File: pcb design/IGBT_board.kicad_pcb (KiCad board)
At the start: 6 copper layers, 150 x 100 mm, 170 parts, among them J1 4-794627-0, Q1 IGBT, Q10 IGBT, Q11 IGBT, Q12 IGBT, Q13 NPN, Q14 PNP, Q15 CSD19533Q5A, Q16 CSD19533Q5A, Q17 NPN, Q18 PNP, Q2 IGBT, Q3 IGBT, Q4 IGBT, Q5 IGBT, Q6 IGBT, Q7 IGBT, Q8 IGBT, Q9 IGBT, T1 TRANS-3-1CT, U1 ISO5852S, U2 LM5030, U3 ISO5852S

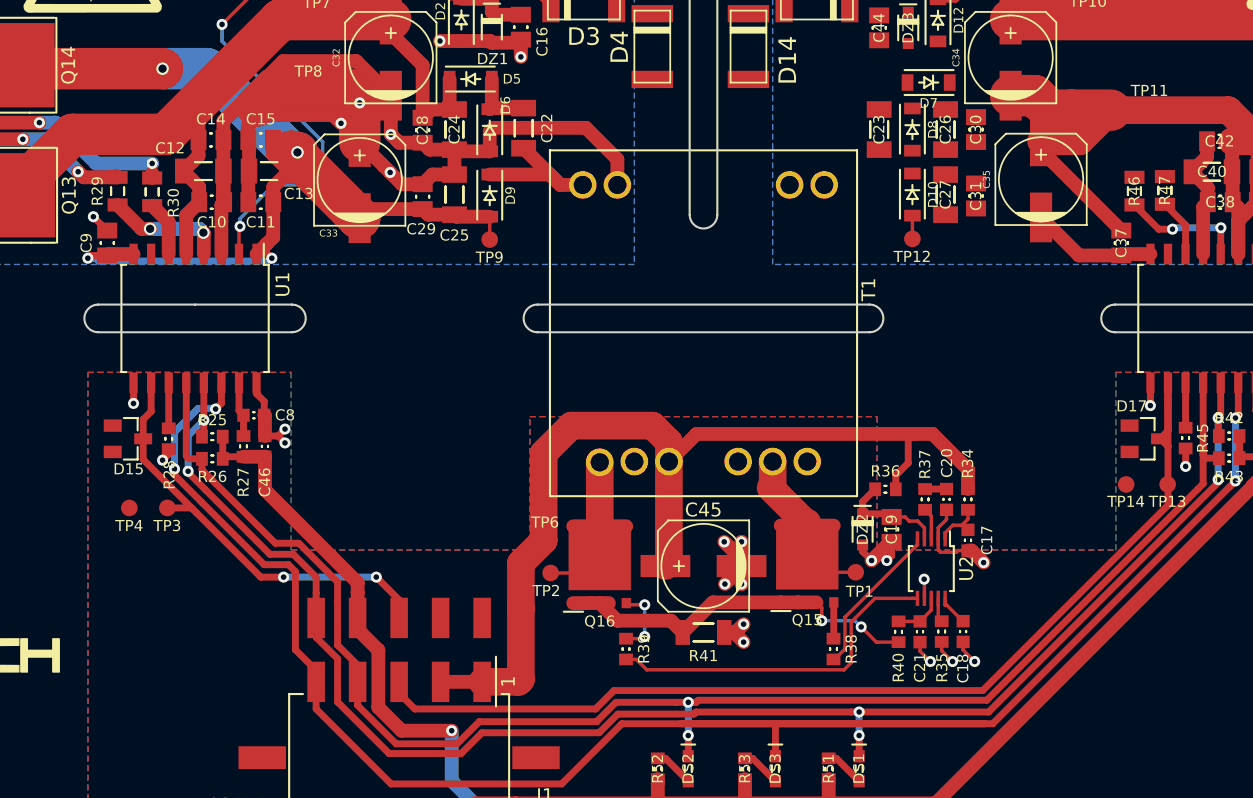
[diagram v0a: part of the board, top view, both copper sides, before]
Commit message: Sync layout with schematic
Signed-off-by: Marcos Chaparro <mchaparro@paltatech.com>
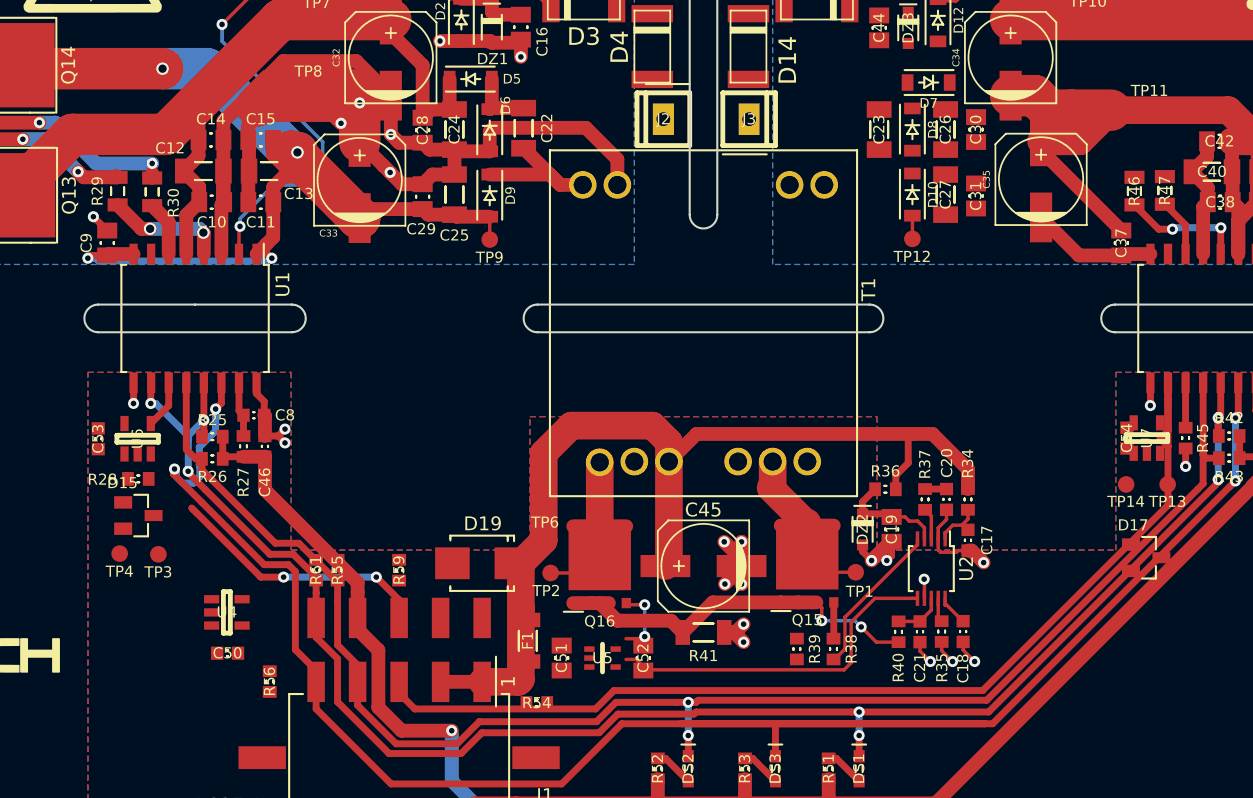
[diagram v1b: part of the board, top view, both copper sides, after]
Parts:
- added C50: 100nF, IPC7351-Nominal:CAPC1608X55, F.Cu at (-34.4, 37.9)
- added C51: 4.7uF, IPC7351-Nominal:CAPC2012X70, F.Cu at (-10.2, 38.2)
- added C52: 4.7uF, IPC7351-Nominal:CAPC2012X70, F.Cu at (-4.35, 38.2)
- added C53: 100nF, IPC7351-Nominal:CAPC1608X55, F.Cu at (-43.8, 22.4)
- added C54: 100nF, IPC7351-Nominal:CAPC1608X55, F.Cu at (30.6, 22.3)
- added D19: TVS, Diodes_SMD:Diode-SMB_Standard, F.Cu at (-16.0, 31.4)
- added F1: FUSE, IPC7351-Nominal:RESC3216X60, F.Cu at (-12.7, 37.0)
- added J2: DESAT, conn-100mil:CONN-100MIL-F-1x1, F.Cu at (-2.90, -0.75)
- added J3: DESAT, conn-100mil:CONN-100MIL-F-1x1, F.Cu at (3.30, -0.75)
- added R54: 22R, IPC7351-Nominal:RESC1608X50, F.Cu at (-12.1, 41.5)
- added R55: 22R, IPC7351-Nominal:RESC1608X50, F.Cu at (-26.4, 31.9)
- added R56: 22R, IPC7351-Nominal:RESC1608X50, F.Cu at (-31.4, 39.9)
- added R59: 22R, IPC7351-Nominal:RESC1608X50, F.Cu at (-22.0, 31.9)
- added R61: 22R, IPC7351-Nominal:RESC1608X50, F.Cu at (-28.0, 31.9)
- added U4: NAND, smd-semi:SOT-23-5, F.Cu at (-34.5, 34.9)
- added U5: APE8865U5-33-HF-3, SC-70-5, F.Cu at (-7.30, 38.2)
- added U6: NAND, smd-semi:SOT-23-5, F.Cu at (-40.9, 22.4)
- added U7: NAND, smd-semi:SOT-23-5, F.Cu at (32.0, 22.3)
- R28, R45: value 0R -> 10k
- R31, R48, R57, R64: value 1R -> 2R
- moved R39 12.3 mm to (6.75, 37.5)
- moved D17 8.60 mm to (32.0, 30.9)
- moved D15 5.60 mm to (-40.9, 27.9)
- moved R28 3.64 mm to (-40.9, 25.2), turned to 0 degrees
- moved TP3 3.41 mm to (-39.4, 30.7)
- moved TP4 3.37 mm to (-42.2, 30.6)
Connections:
- D1 pad 1: GATE_HIGH -> Net-(D1-Pad1)
- D1 pad 2: Net-(D1-Pad2) -> GATE_HIGH
- D11 pad 1: GATE_LOW -> Net-(D11-Pad1)
- D11 pad 2: Net-(D11-Pad2) -> GATE_LOW
- DS2 pad 1: /READY -> /PWR_GOOD
- J1 pad 1: 24v -> Net-(F1-Pad2)
- J1 pad 10: /FAULT -> Net-(J1-Pad10)
- J1 pad 2: 24v -> Net-(F1-Pad2)
- J1 pad 3: /IN_BOTTOM -> Net-(J1-Pad3)
- J1 pad 4: /READY -> Net-(J1-Pad4)
- J1 pad 5: /RESET -> Net-(J1-Pad5)
- J1 pad 6: GND -> Net-(J1-Pad6)
- J1 pad 7: GND -> Net-(J1-Pad6)
- J1 pad 8: /IN_TOP -> Net-(J1-Pad8)
- J1 pad 9: 3.3v -> GND
- R28 pad 1: GND -> /IN_TOP
- R28 pad 2: Net-(R28-Pad2) -> GND
- R43 pad 2: /READY -> /PWR_GOOD
- R45 pad 1: GND -> /IN_BOTTOM
- R45 pad 2: Net-(R45-Pad2) -> GND
- R57 pad 1: Net-(D1-Pad2) -> Net-(D1-Pad1)
- R64 pad 1: Net-(D11-Pad2) -> Net-(D11-Pad1)
- U1 pad 10: /IN_TOP -> /FAULT
- U1 pad 11: Net-(R28-Pad2) -> Net-(U1-Pad11)
- U1 pad 14: /RESET -> /PWR_GOOD
- U3 pad 10: /IN_BOTTOM -> /FAULT
- U3 pad 11: Net-(R45-Pad2) -> Net-(U3-Pad11)
- U3 pad 12: /READY -> /PWR_GOOD
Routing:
- net /READY: track 113.2 -> 16.3 mm, vias 2 -> 0
- net /PWR_GOOD: track 0.00 -> 92.8 mm, vias 0 -> 3
- net Net-(D1-Pad1): track 0.00 -> 38.3 mm
- net GATE_HIGH: track 173.5 -> 139.2 mm
- net /IN_TOP: track 31.7 -> 0.00 mm, vias 2 -> 0
- net /RESET: track 140.1 -> 109.0 mm, vias 4 -> 2
- net Net-(D11-Pad1): track 0.00 -> 25.3 mm
- net Net-(J1-Pad5): track 0.00 -> 23.3 mm, vias 0 -> 1
- net Net-(J1-Pad10): track 0.00 -> 22.5 mm
- net /IN_BOTTOM: track 76.9 -> 54.6 mm, vias 0 -> 1
- net GATE_LOW: track 153.7 -> 132.3 mm
- net Net-(J1-Pad8): track 0.00 -> 19.1 mm, vias 0 -> 2
- net Net-(J1-Pad3): track 0.00 -> 15.5 mm
- net Net-(J1-Pad4): track 0.00 -> 13.5 mm
- net 3.3v: track 117.0 -> 105.6 mm
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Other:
- board text added: "Layers stackup: * Front: gate resistors and IGBT driver * Bottom: IGBT driver ---- 1mm isolation * Ext1: PHASE 1mm copper ---- 1mm isolation * Ext2: VBUS+ 1mm copper ---- 1mm isolation * Ext3: VBUS- 1mm copper"
- board text removed: "Layers stackup: * Front: gate resistors and IGBT driver * In1: IGBT driver ---- 1mm isolation * In2: PHASE 1mm copper ---- 1mm isolation * In3: VBUS+ 1mm copper ---- 1mm isolation * In4: VBUS- 1mm copper"

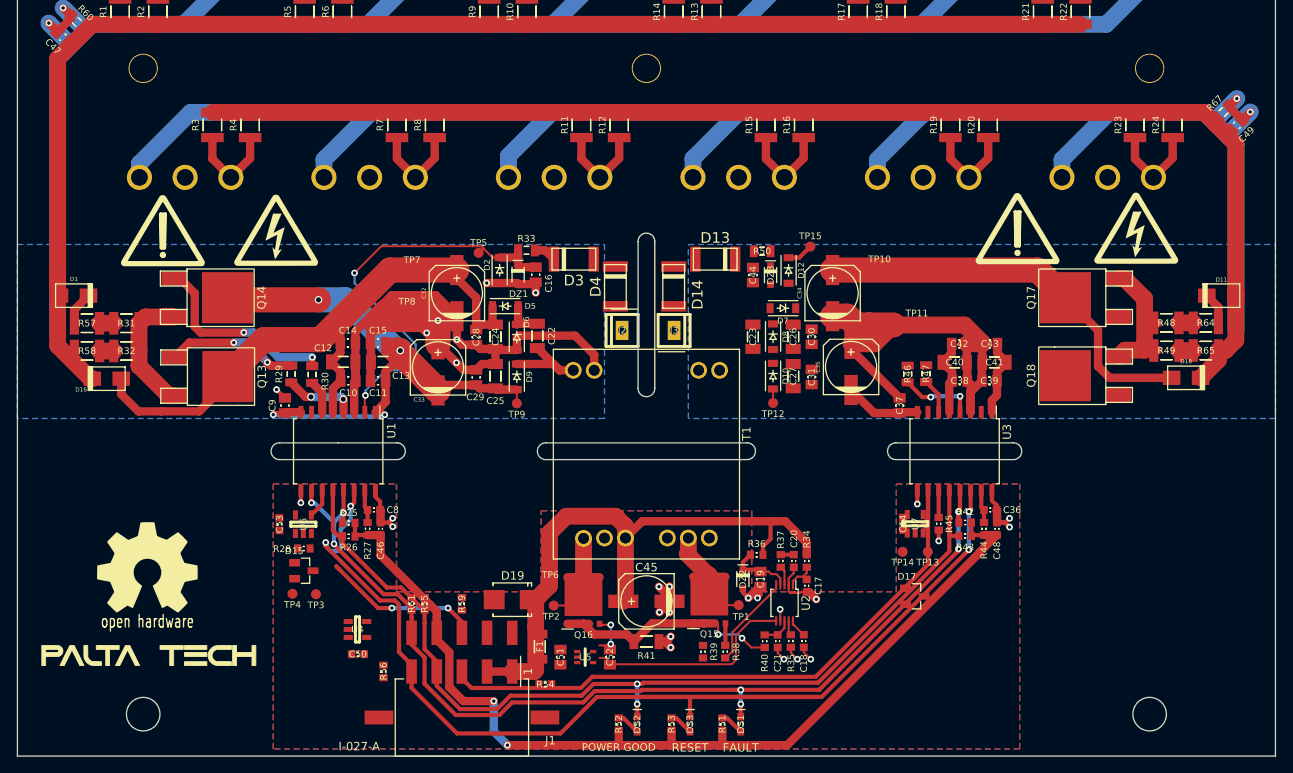
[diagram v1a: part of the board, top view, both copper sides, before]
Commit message: Fixed schematic label and more layout
Signed-off-by: Marcos Chaparro <mchaparro@paltatech.com>
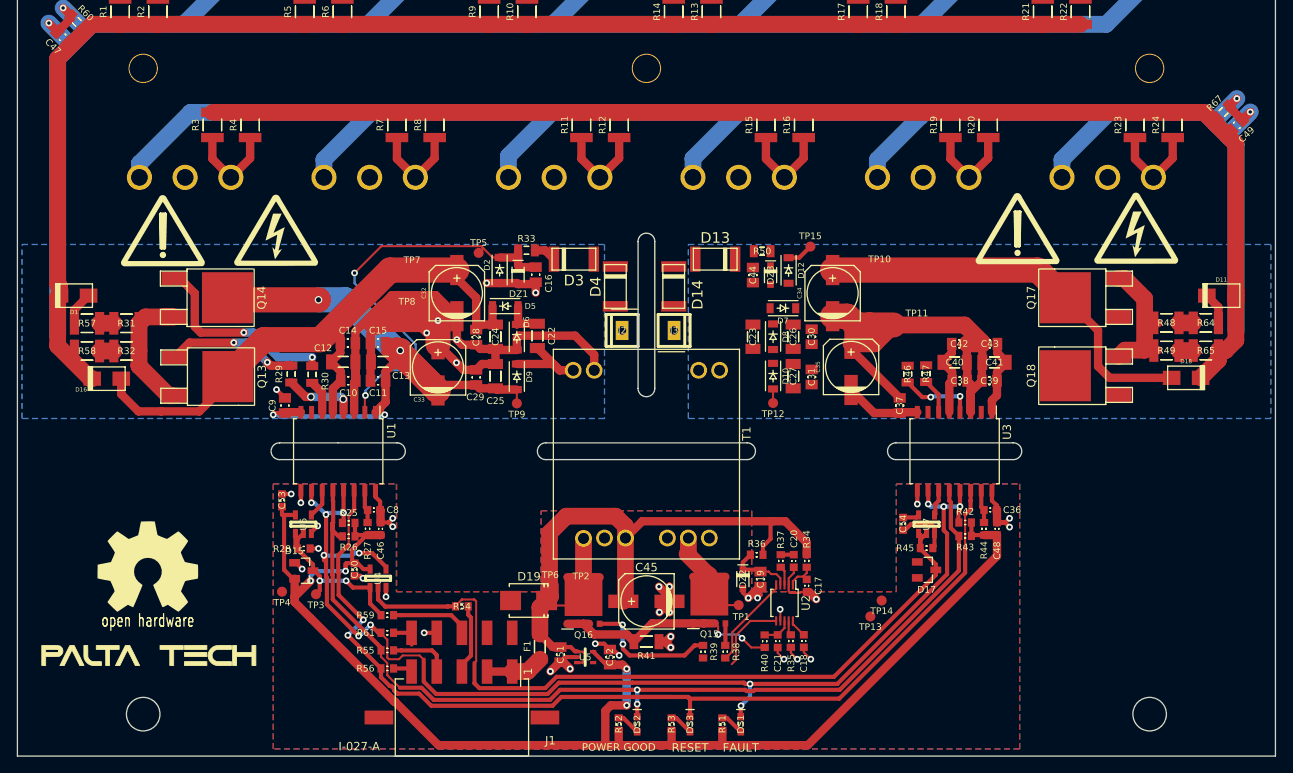
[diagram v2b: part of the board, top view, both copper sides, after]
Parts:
- removed the G*** at (-59.5, 27.5)
- added SYM1: OSHW-SCHEM-PCB10mm, w_logo:Logo_silk_OSHW_12x13mm, F.Cu at (-59.5, 27.4)
- moved R54 13.6 mm to (-22.0, 32.1), turned to 180 degrees
- moved TP13 10.3 mm to (26.7, 33.4)
- moved C50 10.1 mm to (-34.8, 27.8), turned to 270 degrees
- moved R59 9.00 mm to (-30.9, 33.2), turned to 0 degrees
- moved R55 7.11 mm to (-30.9, 37.4), turned to 180 degrees
- moved U4 6.57 mm to (-32.0, 28.8), turned to 90 degrees
- moved TP14 6.32 mm to (28.1, 31.4)
- moved TP2 5.97 mm to (-7.50, 27.2)
- moved R61 4.51 mm to (-30.9, 35.3), turned to 0 degrees
- moved D17 3.45 mm to (33.4, 27.8)
- moved R45 3.24 mm to (33.4, 25.2), turned to 0 degrees
- moved C53 2.87 mm to (-43.5, 19.5)
- moved D19 1.95 mm to (-14.1, 31.4)
- moved U7 1.35 mm to (33.4, 22.4)
- moved TP4 1.27 mm to (-43.5, 30.4)
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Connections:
- J1 pad 6: Net-(J1-Pad6) -> GND
- J1 pad 7: Net-(J1-Pad6) -> GND
- R26 pad 2: /READY -> /PWR_GOOD
- R55 pad 2: /READY -> /PWR_GOOD
- U1 pad 12: /READY -> /PWR_GOOD
- U1 pad 14: /PWR_GOOD -> /RESET
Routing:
- net 3.3v: track 105.6 -> 167.1 mm, vias 2 -> 4
- net /IN_BOTTOM: track 54.6 -> 92.6 mm, vias 1 -> 0
- net /FAULT: track 106.5 -> 141.0 mm, vias 7 -> 12
- net Net-(D1-Pad1): track 38.3 -> 4.00 mm
- net GATE_HIGH: track 139.2 -> 171.2 mm
- net /PWR_GOOD: track 92.8 -> 117.2 mm, vias 3 -> 2
- net /IN_TOP: track 0.00 -> 21.0 mm, vias 0 -> 2
- net Net-(J1-Pad5): track 23.3 -> 3.13 mm, vias 1 -> 0
- net Net-(J1-Pad10): track 22.5 -> 3.55 mm
- net /READY: track 16.3 -> 0.00 mm
- net Net-(R39-Pad1): track 25.2 -> 9.16 mm
- net GND: track 57.4 -> 70.7 mm, vias 19 -> 30
- net /RESET: track 109.0 -> 121.2 mm
- net Net-(Q16-Pad4): track 5.10 -> 16.2 mm
- net Net-(J1-Pad8): track 19.1 -> 9.50 mm, vias 2 -> 0
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
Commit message: Better layout. Added 3d models and updated cache lib
Signed-off-by: Marcos Chaparro <mchaparro@paltatech.com>
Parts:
- removed the G*** at (-59.5, 38.0)
- removed TP15, TP5: DESAT, conn-test:TEST-SMD-SMALL
- added C1: 16uF 700v, paltatech:CAP_FILM_EPCOS_42x20mm_3D_only, B.Cu at (-61.5, 14.9)
- added C2: 16uF 700v, paltatech:CAP_FILM_EPCOS_42x20mm_3D_only, B.Cu at (-41.0, 14.9)
- added C3: 16uF 700v, paltatech:CAP_FILM_EPCOS_42x20mm_3D_only, B.Cu at (-20.5, 14.9)
- added C4: 16uF 700v, paltatech:CAP_FILM_EPCOS_42x20mm_3D_only, B.Cu at (0.00, 15.0)
- added C5: 16uF 700v, paltatech:CAP_FILM_EPCOS_42x20mm_3D_only, B.Cu at (20.5, 15.0)
- added C55: 1nF, IPC7351-Nominal:CAPC1608X55, F.Cu at (182.4, 36.9)
- added C56: 1uF, IPC7351-Nominal:CAPC1608X55, F.Cu at (175.2, 43.5)
- added C57: 10uF 50v, IPC7351-Nominal:CAPC3216X70, F.Cu at (168.4, 42.7)
- added C58: 10uF 50v, IPC7351-Nominal:CAPC3216X70, F.Cu at (168.4, 37.3)
- added C59: 10nF, IPC7351-Nominal:CAPC1608X55, F.Cu at (142.2, 53.0)
- added C6: 16uF 700v, paltatech:CAP_FILM_EPCOS_42x20mm_3D_only, B.Cu at (41.0, 15.0)
- added C60: 100nF, IPC7351-Nominal:CAPC1608X55, F.Cu at (154.3, 36.9)
- added C61: 10nF, IPC7351-Nominal:CAPC1608X55, F.Cu at (142.2, 48.5)
- added C62: 47uF 50v, w_smd_cap:c_elec_6.3x7.7, F.Cu at (134.8, 40.5)
- added C63: 1nF, IPC7351-Nominal:CAPC1608X55, F.Cu at (203.9, 41.2)
- added C64: 1uF, IPC7351-Nominal:CAPC1608X55, F.Cu at (37.6, 17.6)
- added C65: 10uF 50v, IPC7351-Nominal:CAPC3216X70, F.Cu at (46.7, 4.30)
- added C66: 10uF 50v, IPC7351-Nominal:CAPC3216X70, F.Cu at (64.7, 4.30)
- added C67: 10nF, IPC7351-Nominal:CAPC1608X55, F.Cu at (31.4, 7.10)
- added C68: 100nF, IPC7351-Nominal:CAPC1608X55, F.Cu at (37.0, 4.40)
- added C69: 10nF, IPC7351-Nominal:CAPC1608X55, F.Cu at (40.6, 11.9)
- added C7: 16uF 700v, paltatech:CAP_FILM_EPCOS_42x20mm_3D_only, B.Cu at (61.5, 15.0)
- added C70: 47uF 50v, w_smd_cap:c_elec_6.3x7.7, F.Cu at (40.6, -1.65)
- added C71: 10uF 50v, IPC7351-Nominal:CAPC3216X70, F.Cu at (119.4, 75.9)
- added C72: 10uF 50v, IPC7351-Nominal:CAPC3216X70, F.Cu at (127.1, 75.9)
- added C73: 10uF 50v, IPC7351-Nominal:CAPC3216X70, F.Cu at (46.7, 9.05)
- added C74: 10uF 50v, IPC7351-Nominal:CAPC3216X70, F.Cu at (64.7, 9.05)
- added DS4: CAPS_CHARGED, smd-semi:LED-0603, F.Cu at (-51.6, 132.4)
- added DZ4: 10v, smd-semi:SOT-23, F.Cu at (175.8, 38.0)
- added DZ5: 10v, smd-semi:SOT-23, F.Cu at (37.6, 15.0)
- added Q19: PNP, SMD_Packages:DPAK-2, F.Cu at (123.8, 47.3)
- added Q20: PNP, SMD_Packages:DPAK-2, F.Cu at (33.5, 1.45)
- added R62: 50k 1W, IPC7351-Nominal:RESC6432X70, F.Cu at (-40.0, 133.5)
- added R63: 50k 1W, IPC7351-Nominal:RESC6432X70, F.Cu at (38.2, 87.1)
- added R66: 50k 1W, IPC7351-Nominal:RESC6432X70, F.Cu at (-29.1, 133.5)
- added R68: 380R, IPC7351-Nominal:RESC1608X50, F.Cu at (181.2, 43.6)
- added R69: 470R, IPC7351-Nominal:RESC1608X50, F.Cu at (187.1, 41.4)
- added R70: 10k, IPC7351-Nominal:RESC1608X50, F.Cu at (148.2, 50.4)
- added R71: 10k, IPC7351-Nominal:RESC1608X50, F.Cu at (148.2, 45.8)
- added R72: 10k, IPC7351-Nominal:RESC1608X50, F.Cu at (154.3, 41.4)
- added R73: 100R, IPC7351-Nominal:RESC2012X50, F.Cu at (122.6, 53.6)
- added R74: 380R, IPC7351-Nominal:RESC1608X50, F.Cu at (34.7, 17.3)
- added R75: 470R, IPC7351-Nominal:RESC1608X50, F.Cu at (34.7, 14.3)
- added R76: 10k, IPC7351-Nominal:RESC1608X50, F.Cu at (34.6, 11.9)
- added R77: 10k, IPC7351-Nominal:RESC1608X50, F.Cu at (33.0, 7.10)
- added R78: 10k, IPC7351-Nominal:RESC1608X50, F.Cu at (37.6, 11.9)
- added R79: 100R, IPC7351-Nominal:RESC2012X50, F.Cu at (41.2, 4.40)
- added R80: NI, IPC7351-Nominal:RESC3216X60, F.Cu at (112.8, 19.2)
- added U11: TLP2745, paltatech:SDIP6, F.Cu at (37.6, 25.0)
- added U12: OPA2172, IPC7351-Nominal:SOIC127P600X175-8, F.Cu at (37.6, 8.30)
- added U8: TLP2745, paltatech:SDIP6, F.Cu at (175.7, 48.7)
- added U9: OPA2172, IPC7351-Nominal:SOIC127P600X175-8, F.Cu at (132.5, 53.0)
- moved D14 67.7 mm to (70.2, 3.50), turned to 270 degrees
- moved J3 67.0 mm to (70.2, -2.00), turned to 90 degrees
- moved D13 65.0 mm to (70.2, 10.0), turned to 270 degrees
- moved C44 62.2 mm to (69.0, 19.0)
- moved R50 60.8 mm to (69.0, 15.2), turned to 270 degrees
- moved DZ3 58.3 mm to (66.8, 19.0)
- moved D12 54.2 mm to (63.2, 20.2), turned to 0 degrees
- moved G*** 38.4 mm to (25.2, -32.2)
- moved G*** 35.1 mm to (67.7, -39.1)
- moved R47 32.3 mm to (64.1, 14.2)
- moved C38 21.2 mm to (55.0, 17.1)
- moved C39 21.2 mm to (58.5, 17.1)
- moved C40 21.2 mm to (54.4, 14.9)
- moved C41 21.2 mm to (59.1, 14.9)
- moved C42 21.2 mm to (54.9, 12.7)
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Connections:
- C11 pad 2: /IGBT_driver_TOP/-8V -> /IGBT_driver_TOP/-VEE
- C13 pad 2: /IGBT_driver_TOP/-8V -> /IGBT_driver_TOP/-VEE
- C15 pad 2: /IGBT_driver_TOP/-8V -> /IGBT_driver_TOP/-VEE
- C37 pad 2: /IGBT_driver_BOT/-8V -> /IGBT_driver_BOT/-VEE
- C39 pad 2: /IGBT_driver_BOT/-8V -> /IGBT_driver_BOT/-VEE
- C41 pad 2: /IGBT_driver_BOT/-8V -> /IGBT_driver_BOT/-VEE
- C43 pad 2: /IGBT_driver_BOT/-8V -> /IGBT_driver_BOT/-VEE
- C9 pad 2: /IGBT_driver_TOP/-8V -> /IGBT_driver_TOP/-VEE
- D1 pad 1: Net-(D1-Pad1) -> GATE_HIGH
- D1 pad 2: GATE_HIGH -> /IGBT_driver_TOP/-VEE
- D11 pad 1: Net-(D11-Pad1) -> GATE_LOW
- D11 pad 2: GATE_LOW -> /IGBT_driver_BOT/-VEE
- Q14 pad 2: /IGBT_driver_TOP/-8V -> /IGBT_driver_TOP/-VEE
- Q14 pad 3: Net-(Q13-Pad3) -> Net-(Q14-Pad3)
- Q18 pad 2: /IGBT_driver_BOT/-8V -> /IGBT_driver_BOT/-VEE
- Q18 pad 3: Net-(Q17-Pad3) -> Net-(Q18-Pad3)
- R32 pad 2: Net-(Q13-Pad3) -> Net-(Q14-Pad3)
- R49 pad 2: Net-(Q17-Pad3) -> Net-(Q18-Pad3)
- R57 pad 1: Net-(D1-Pad1) -> GATE_HIGH
- R64 pad 1: Net-(D11-Pad1) -> GATE_LOW
- U1 pad 1: /IGBT_driver_TOP/-8V -> /IGBT_driver_TOP/-VEE
- U1 pad 8: /IGBT_driver_TOP/-8V -> /IGBT_driver_TOP/-VEE
- U3 pad 1: /IGBT_driver_BOT/-8V -> /IGBT_driver_BOT/-VEE
- U3 pad 8: /IGBT_driver_BOT/-8V -> /IGBT_driver_BOT/-VEE
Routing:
- net VBUS-: track 283.5 -> 372.1 mm, vias 2 -> 60
- net /IGBT_driver_BOT/-VEE: track 0.00 -> 82.2 mm, vias 0 -> 15
- net /IGBT_driver_TOP/-VEE: track 0.00 -> 64.5 mm, vias 0 -> 4
- net /IGBT_driver_TOP/-8V: track 79.1 -> 28.5 mm, vias 4 -> 0
- net /IGBT_driver_BOT/-8V: track 20.1 -> 68.0 mm, vias 0 -> 2
- net /IGBT_driver_BOT/+15V: track 63.1 -> 108.8 mm, vias 0 -> 22
- net PHASE: track 333.6 -> 300.0 mm
- net 3.3v: track 167.1 -> 133.6 mm
- net /RESET: track 121.2 -> 89.9 mm
- net Net-(D11-Pad1): track 25.3 -> 0.00 mm
- net GATE_LOW: track 132.3 -> 156.5 mm
- net Net-(Q17-Pad3): track 28.7 -> 5.35 mm
- net Net-(Q17-Pad1): track 0.00 -> 22.5 mm
- net /PWR_GOOD: track 117.2 -> 97.1 mm
- net Net-(Q18-Pad1): track 0.00 -> 19.7 mm
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- added copper zone on GNDs.Cu, net PHASE
- added copper zone on PWR.Cu, net VBUS+
- removed copper zone on Ext1(PHASE).Cu, net PHASE
- removed copper zone on Ext2(VBUS+).Cu, net VBUS+
- removed copper zone on Ext3(VBUS-).Cu, net VBUS-
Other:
- outline, holes or cut-outs redrawn
- copper layers 6 -> 4
- board text added: "Capacitive coupling between bottom gnd and bottom-er phase copper plane is calculated this way: C=(4.7)(8.854×10−12)A(1.6×10−3) So, in this case with 1mm separator: (4.7*8.854*10^-12*0.09*0.03)/0.001 = 112pF"
- board text removed: "Capacitive coumpling between bottom gnd and bottom-er phase copper plane is calculated this way: C=(4.7)(8.854×10−12)A(1.6×10−3) So, in this case with 1mm separator: (4.7*8.854*10^-12*0.09*0.03)/0.001 = 112pF"
